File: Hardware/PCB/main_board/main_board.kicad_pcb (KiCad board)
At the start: 2 copper layers, 16 parts, among them Q1 BC547, U1 MCP6002-xSN

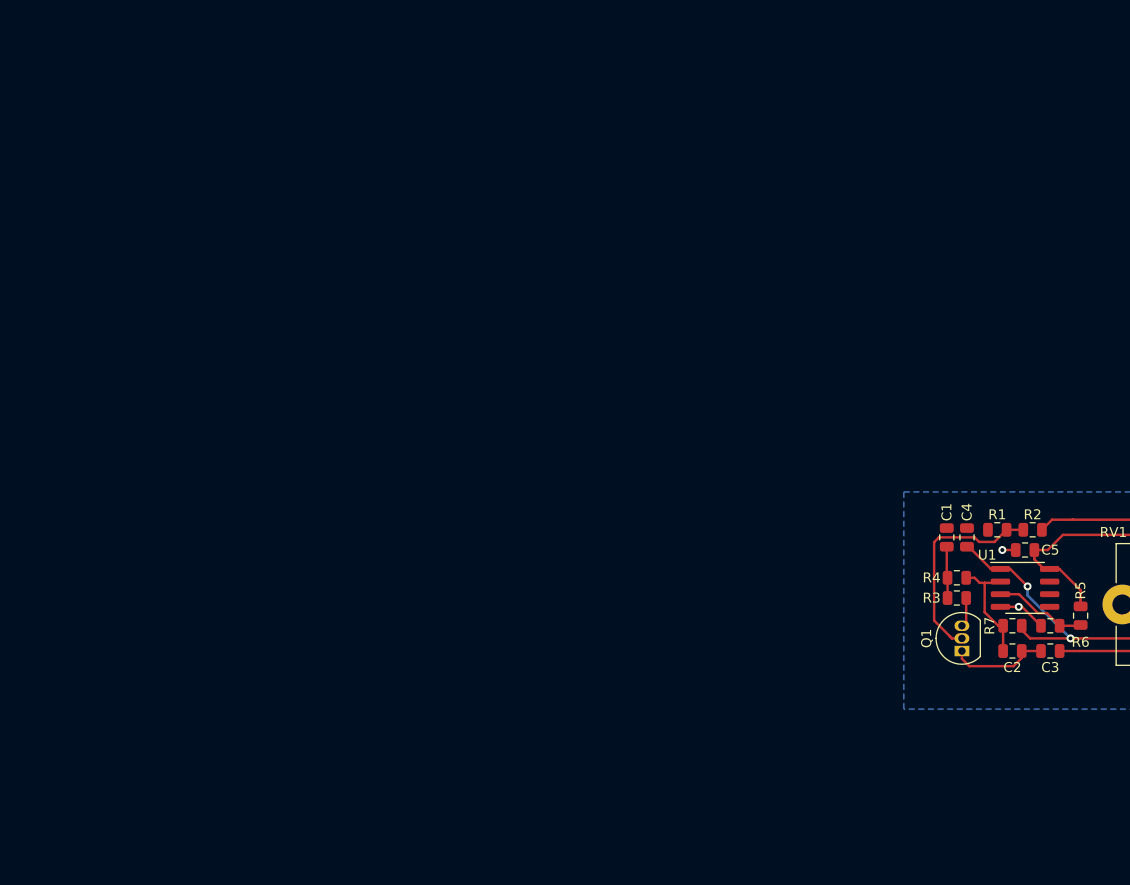
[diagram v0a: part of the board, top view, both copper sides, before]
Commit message: Add NUCLEO footprint
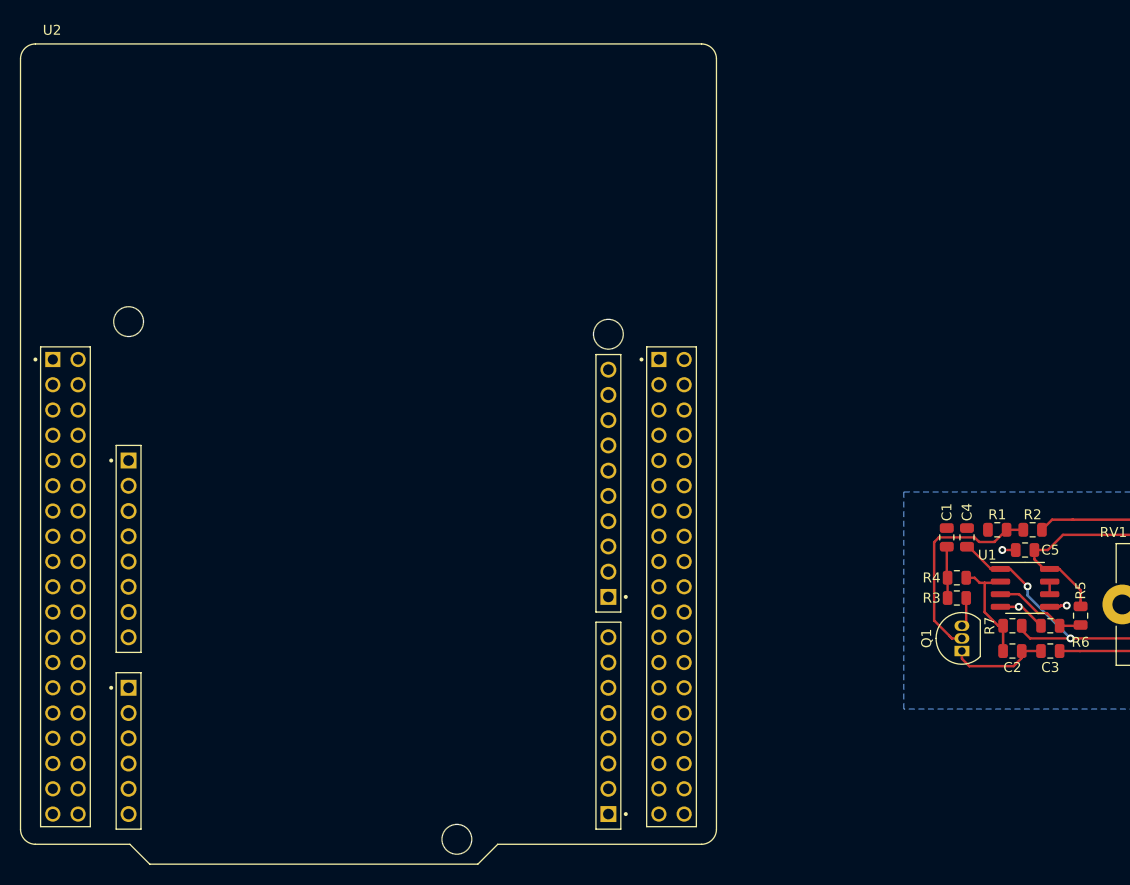
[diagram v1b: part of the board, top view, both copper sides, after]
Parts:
- added U2: NUCLEO-F446RE, MODULE_NUCLEO-F446RE, F.Cu at (-488.9, -323.3)
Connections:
- net AUDIO_OUT renamed /analog/AUDIO_OUT
- C1 pad 2: AUDIO_IN -> /analog/AUDIO_IN
- R1 pad 2: CV_IN -> /analog/CV_IN
- U1 pad 5: Net-(U1-Pad5) -> GND
- U1 pad 7: Net-(U1-Pad7) -> Net-(U1-Pad6)
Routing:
- net GND: track 9.19 -> 11.0 mm, vias 2 -> 3
- net Net-(U1-Pad6): track 0.00 -> 1.27 mm

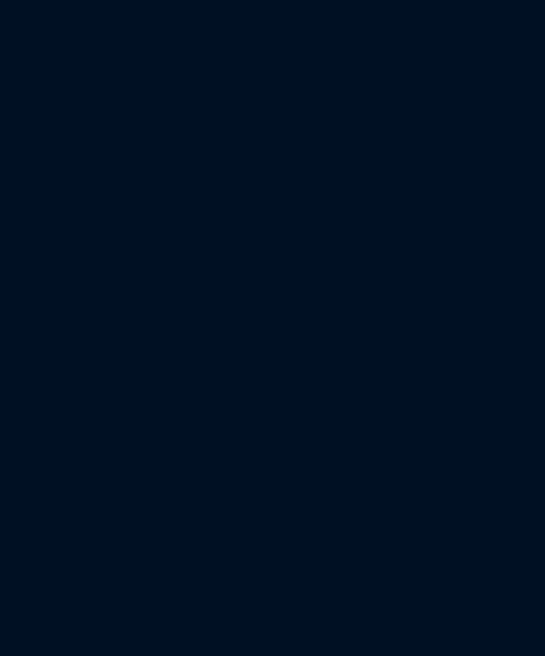
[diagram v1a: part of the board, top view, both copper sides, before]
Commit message: Add programming connector to PCB
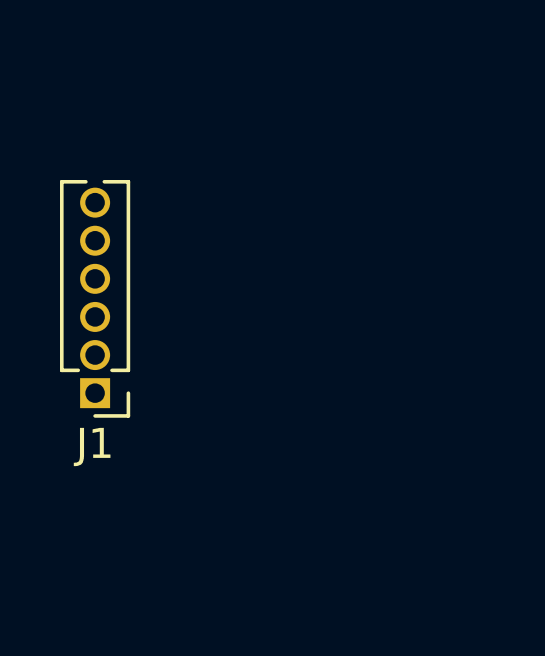
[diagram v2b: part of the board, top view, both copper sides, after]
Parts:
- added J1: SWD, Connector_PinHeader_1.27mm:PinHeader_1x06_P1.27mm_Vertical, F.Cu at (-548.5, -296.9)
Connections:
- U2 pad CN10_31: Net-(U2-PadCN10_31) -> /MCU/SWO
- U2 pad CN7_13: Net-(U2-PadCN7_13) -> /MCU/SWDIO
- U2 pad CN7_14: Net-(U2-PadCN7_14) -> /MCU/NRST
- U2 pad CN7_15: Net-(U2-PadCN7_15) -> /MCU/SWCLK

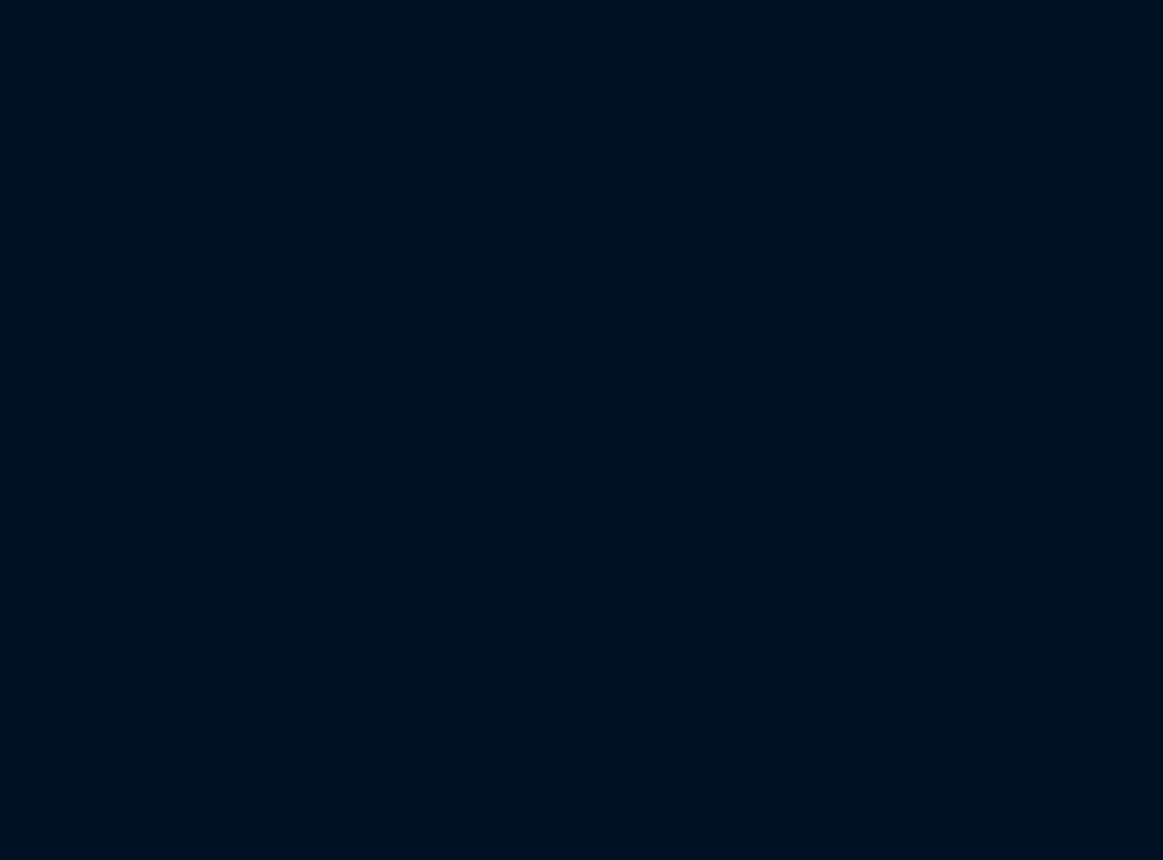
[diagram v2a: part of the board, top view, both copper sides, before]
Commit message: Add MIDI hardware
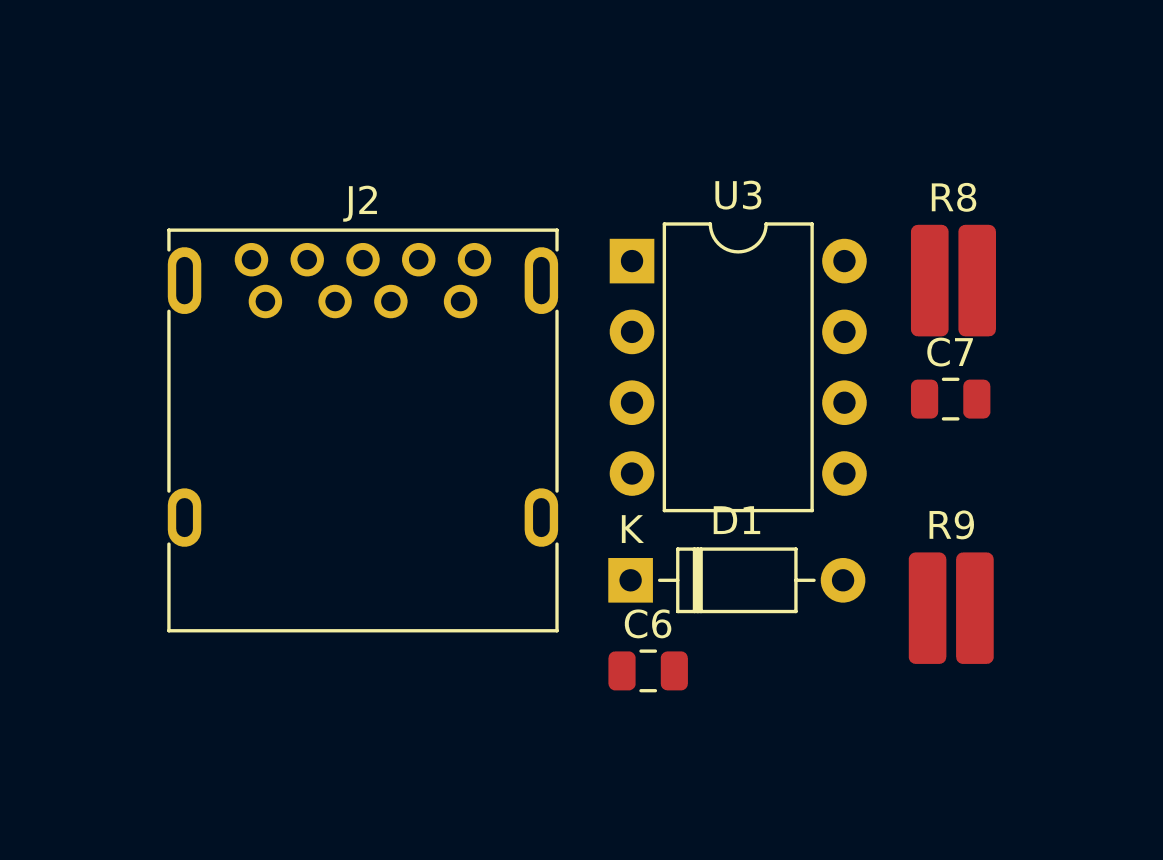
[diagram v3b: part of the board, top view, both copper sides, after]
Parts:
- added C6: 100n, Capacitor_SMD:C_0805_2012Metric, F.Cu at (-424.8, -343.5)
- added C7: 100n, Capacitor_SMD:C_0805_2012Metric, F.Cu at (-414.0, -353.3)
- added D1: 1N4148, Diode_THT:D_DO-35_SOD27_P7.62mm_Horizontal, F.Cu at (-425.4, -346.8)
- added J2: USB_A, Connector_USB:USB3_A_Molex_48393-001, F.Cu at (-438.5, -356.8)
- added R8: 220, Resistor_SMD:R_0815_2038Metric, F.Cu at (-413.9, -357.5)
- added R9: 10k, Resistor_SMD:R_0815_2038Metric, F.Cu at (-413.9, -345.8)
- added U3: 6N137, Package_DIP:DIP-8_W7.62mm, F.Cu at (-425.4, -358.2)
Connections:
- net /analog/AUDIO_IN renamed /analogFX/AUDIO_IN
- net /analog/AUDIO_OUT renamed /analogFX/AUDIO_OUT
- net /analog/CV_IN renamed /analogFX/CV_IN

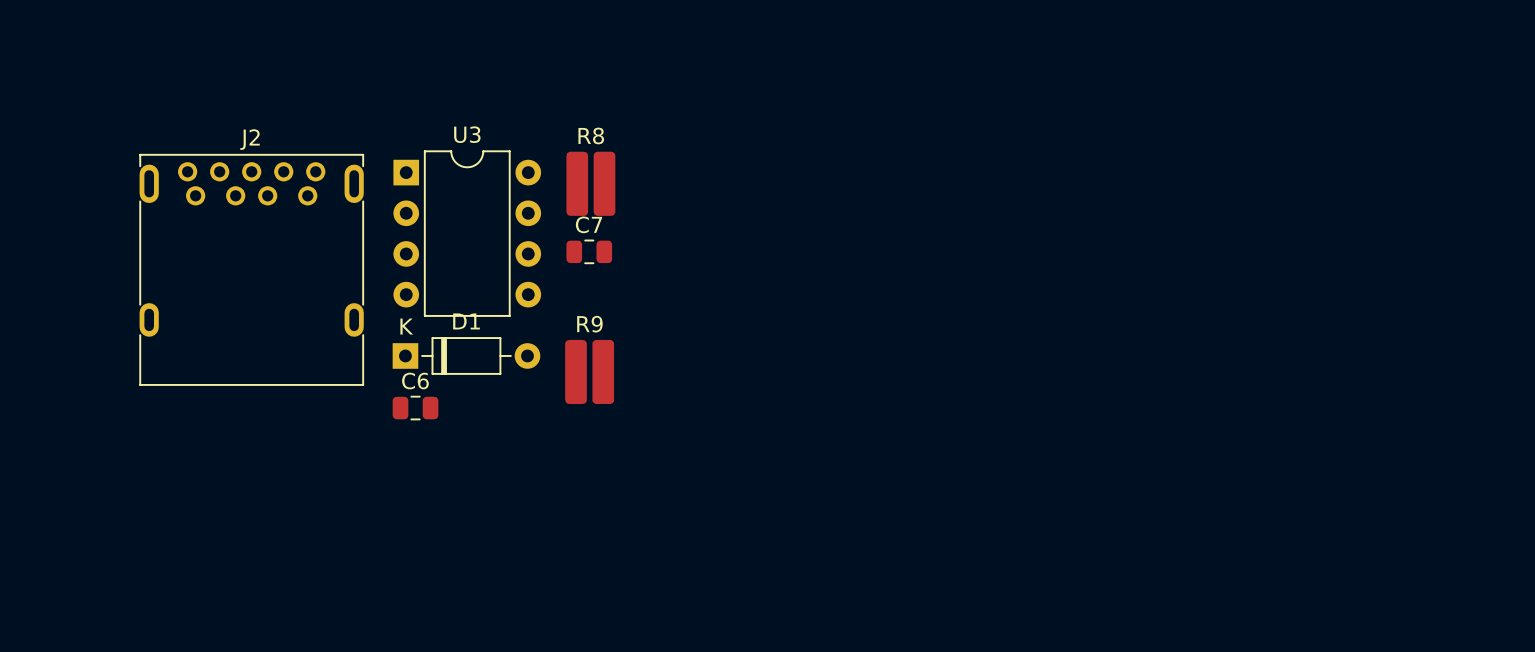
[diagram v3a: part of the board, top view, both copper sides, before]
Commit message: Add power supply schematics and layout
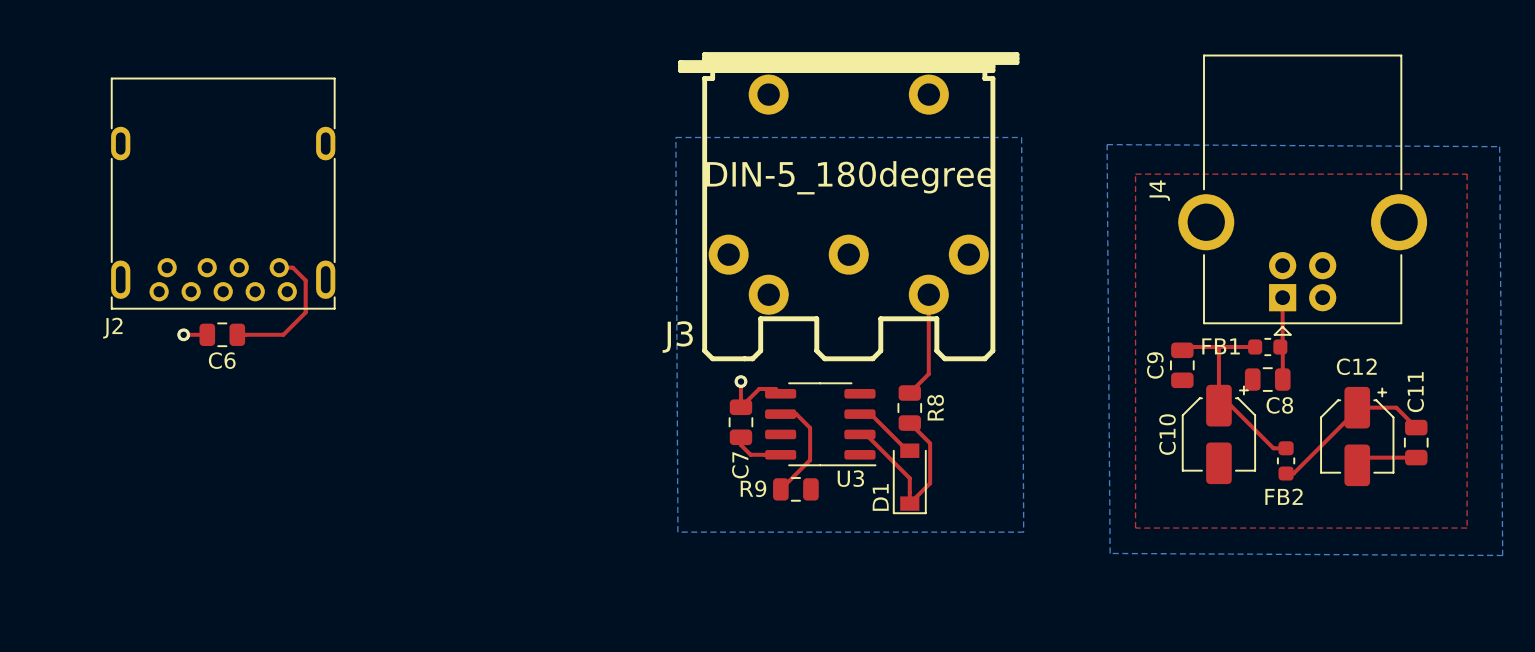
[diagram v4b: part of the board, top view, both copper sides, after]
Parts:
- added C10: 4.7u, Capacitor_SMD:CP_Elec_4x5.4, F.Cu at (-374.6, -341.9)
- added C11: 100n, Capacitor_SMD:C_0805_2012Metric, F.Cu at (-362.3, -341.4)
- added C12: 4.7u, Capacitor_SMD:CP_Elec_4x5.4, F.Cu at (-366.0, -341.8)
- added C8: 10n, Capacitor_SMD:C_0805_2012Metric, F.Cu at (-371.6, -345.3)
- added C9: 100n, Capacitor_SMD:C_0805_2012Metric, F.Cu at (-376.9, -346.2)
- added FB1: BLM18pg221sn1d - Ferrite_Bead, Inductor_SMD:L_0603_1608Metric, F.Cu at (-371.6, -347.3)
- added FB2: BLM18pg221sn1d - Ferrite_Bead, Inductor_SMD:L_0603_1608Metric, F.Cu at (-370.5, -340.2)
- added J3: DIN-5_180degree, lib:MIDI_DIN5, F.Cu at (-397.8, -356.1)
- added J4: USB_B, Connector_USB:USB_B_OST_USB-B1HSxx_Horizontal, F.Cu at (-370.7, -350.4)
- D1: footprint Diode_THT:D_DO-35_SOD27_P7.62mm_Horizontal -> Diode_SMD:D_SOD-123
- R8, R9: footprint Resistor_SMD:R_0815_2038Metric -> Resistor_SMD:R_0805_2012Metric
- U2: footprint MODULE_NUCLEO-F446RE -> lib:MODULE_NUCLEO-F446RE
- U3: footprint Package_DIP:DIP-8_W7.62mm -> Package_SO:SOIC-8_3.9x4.9mm_P1.27mm
- moved D1 32.4 mm to (-394.0, -339.2), turned to 90 degrees
- moved U3 30.3 mm to (-399.5, -342.5), turned to 180 degrees
- moved R8 24.3 mm to (-394.0, -343.5), turned to 90 degrees
- moved R9 14.8 mm to (-401.1, -338.5), turned to 180 degrees
- moved C7 14.2 mm to (-404.5, -342.6), turned to 90 degrees
- moved C6 12.9 mm to (-436.9, -348.1), turned to 180 degrees
- moved J2 6.88 mm to (-433.3, -352.3), turned to 180 degrees
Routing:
- net +5V: track 0.00 -> 27.9 mm
- net Net-(D1-Pad1): track 0.00 -> 11.9 mm
- net GND: track 11.0 -> 21.5 mm, vias 3 -> 5
- net +5VA: track 19.9 -> 30.3 mm
- net Net-(R9-Pad2): track 0.00 -> 6.79 mm
- net Net-(J3-Pad5): track 0.00 -> 6.63 mm
- net Net-(C8-Pad1): track 0.00 -> 5.23 mm
- net Net-(D1-Pad2): track 0.00 -> 4.06 mm
- added copper zone on F.Cu, net GND

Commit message: Add OLED screen to PCB
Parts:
- added Brd1: SSD1306, lib:128x64OLED, F.Cu at (-427.1, -270.1)
- added Brd2: SSD1306, lib:128x64OLED, F.Cu at (-398.6, -270.1)
- added C13: 100n, Capacitor_SMD:C_0805_2012Metric, F.Cu at (-429.4, -284.0)
- added C14: 100n, Capacitor_SMD:C_0805_2012Metric, F.Cu at (-401.1, -284.0)
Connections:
- net Net-(U2-PadCN7_16) renamed +3V3

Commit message: Add HMI buttons and pots to PCB
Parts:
- added RV10: 10k, Potentiometer_THT:Potentiometer_Alps_RK09K_Single_Vertical, F.Cu at (-308.4, -275.6)
- added RV11: 10k, Potentiometer_THT:Potentiometer_Alps_RK09K_Single_Vertical, F.Cu at (-323.9, -246.9)
- added RV12: 10k, Potentiometer_THT:Potentiometer_Alps_RK09K_Single_Vertical, F.Cu at (-308.4, -261.2)
- added RV13: 10k, Potentiometer_THT:Potentiometer_Alps_RK09K_Single_Vertical, F.Cu at (-293.0, -275.6)
- added RV14: 10k, Potentiometer_THT:Potentiometer_Alps_RK09K_Single_Vertical, F.Cu at (-308.4, -246.9)
- added RV3: 10k, Potentiometer_THT:Potentiometer_Alps_RK09K_Single_Vertical, F.Cu at (-355.2, -275.7)
- added RV4: 10k, Potentiometer_THT:Potentiometer_Alps_RK09K_Single_Vertical, F.Cu at (-355.2, -261.4)
- added RV5: 10k, Potentiometer_THT:Potentiometer_Alps_RK09K_Single_Vertical, F.Cu at (-339.8, -275.7)
- added RV6: 10k, Potentiometer_THT:Potentiometer_Alps_RK09K_Single_Vertical, F.Cu at (-339.8, -261.4)
- added RV7: 10k, Potentiometer_THT:Potentiometer_Alps_RK09K_Single_Vertical, F.Cu at (-293.0, -261.2)
- added RV8: 10k, Potentiometer_THT:Potentiometer_Alps_RK09K_Single_Vertical, F.Cu at (-323.9, -275.6)
- added RV9: 10k, Potentiometer_THT:Potentiometer_Alps_RK09K_Single_Vertical, F.Cu at (-323.9, -261.2)
- added SW1: SW_Push, Button_Switch_THT:SW_PUSH_6mm_H13mm, F.Cu at (-266.6, -283.2)
- added SW10: SW_Push, Button_Switch_THT:SW_PUSH_6mm_H13mm, F.Cu at (-271.5, -249.0)
- added SW11: SW_Push, Button_Switch_THT:SW_PUSH_6mm_H13mm, F.Cu at (-261.0, -257.6)
- added SW2: SW_Push, Button_Switch_THT:SW_PUSH_6mm_H13mm, F.Cu at (-277.2, -274.7)
- added SW3: SW_Push, Button_Switch_THT:SW_PUSH_6mm_H13mm, F.Cu at (-277.2, -283.2)
- added SW4: SW_Push, Button_Switch_THT:SW_PUSH_6mm_H13mm, F.Cu at (-292.6, -254.5)
- added SW5: SW_Push, Button_Switch_THT:SW_PUSH_6mm_H13mm, F.Cu at (-266.6, -274.7)
- added SW6: SW_Push, Button_Switch_THT:SW_PUSH_6mm_H13mm, F.Cu at (-277.2, -266.1)
- added SW7: SW_Push, Button_Switch_THT:SW_PUSH_6mm_H13mm, F.Cu at (-282.1, -254.5)
- added SW8: SW_Push, Button_Switch_THT:SW_PUSH_6mm_H13mm, F.Cu at (-266.6, -266.1)
- added SW9: SW_Push, Button_Switch_THT:SW_PUSH_6mm_H13mm, F.Cu at (-271.5, -257.6)
- moved C13 26.7 mm to (-402.8, -286.4)
- moved Brd1 26.7 mm to (-400.6, -272.5)
- moved Brd2 26.7 mm to (-372.0, -272.5)
- moved C14 26.7 mm to (-374.5, -286.4)
